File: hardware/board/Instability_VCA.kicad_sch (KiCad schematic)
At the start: 30 parts

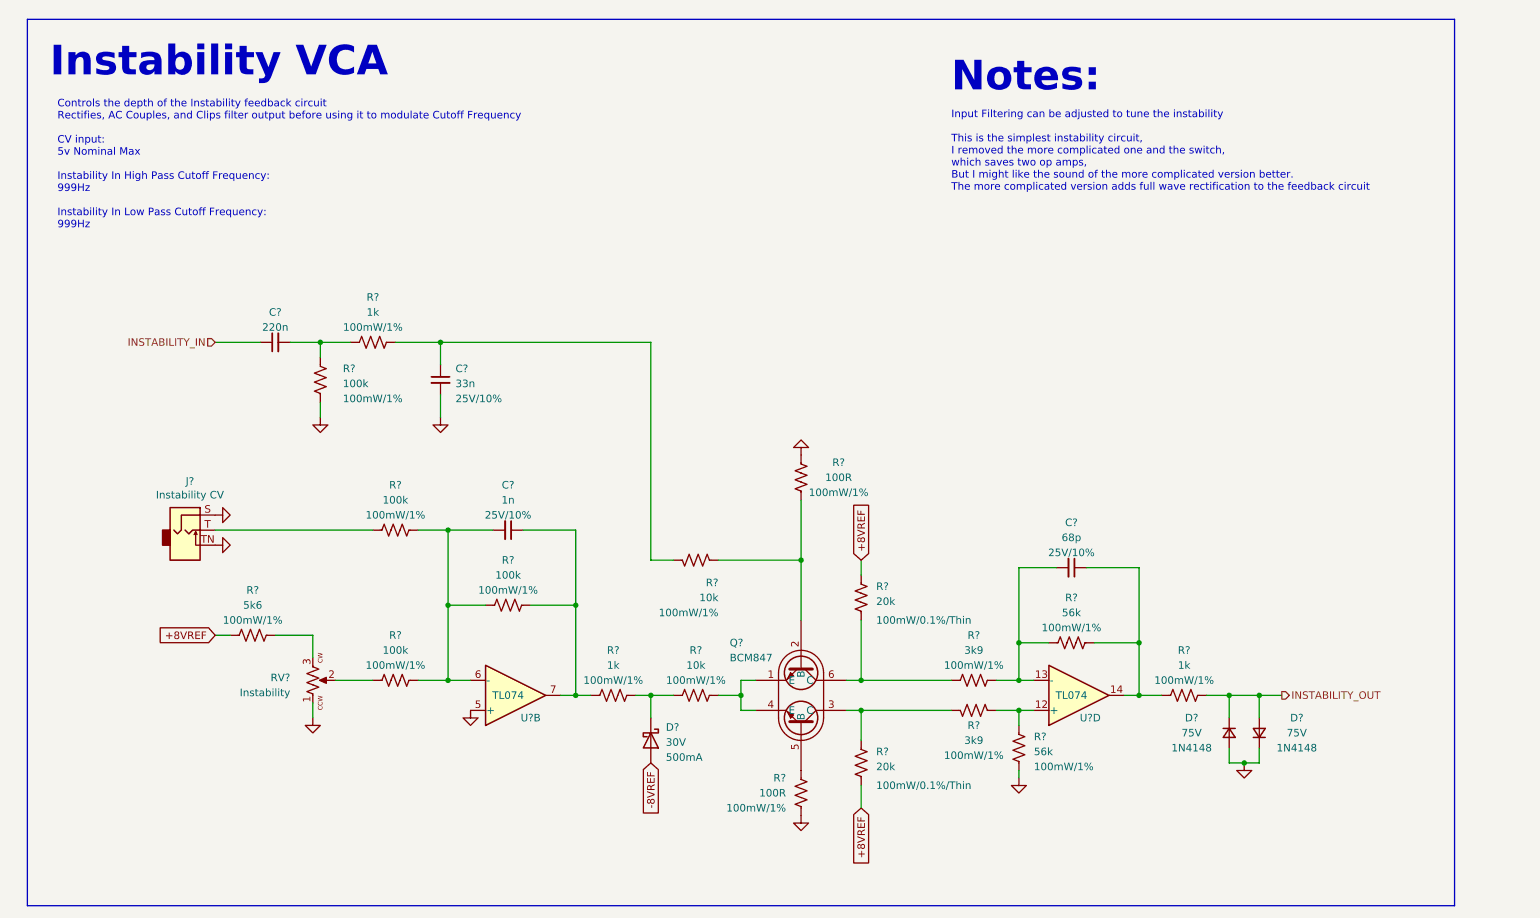
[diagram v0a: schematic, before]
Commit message: Schematic getting closer to being finished
Schematic should be close to being ready to assign MPNs.
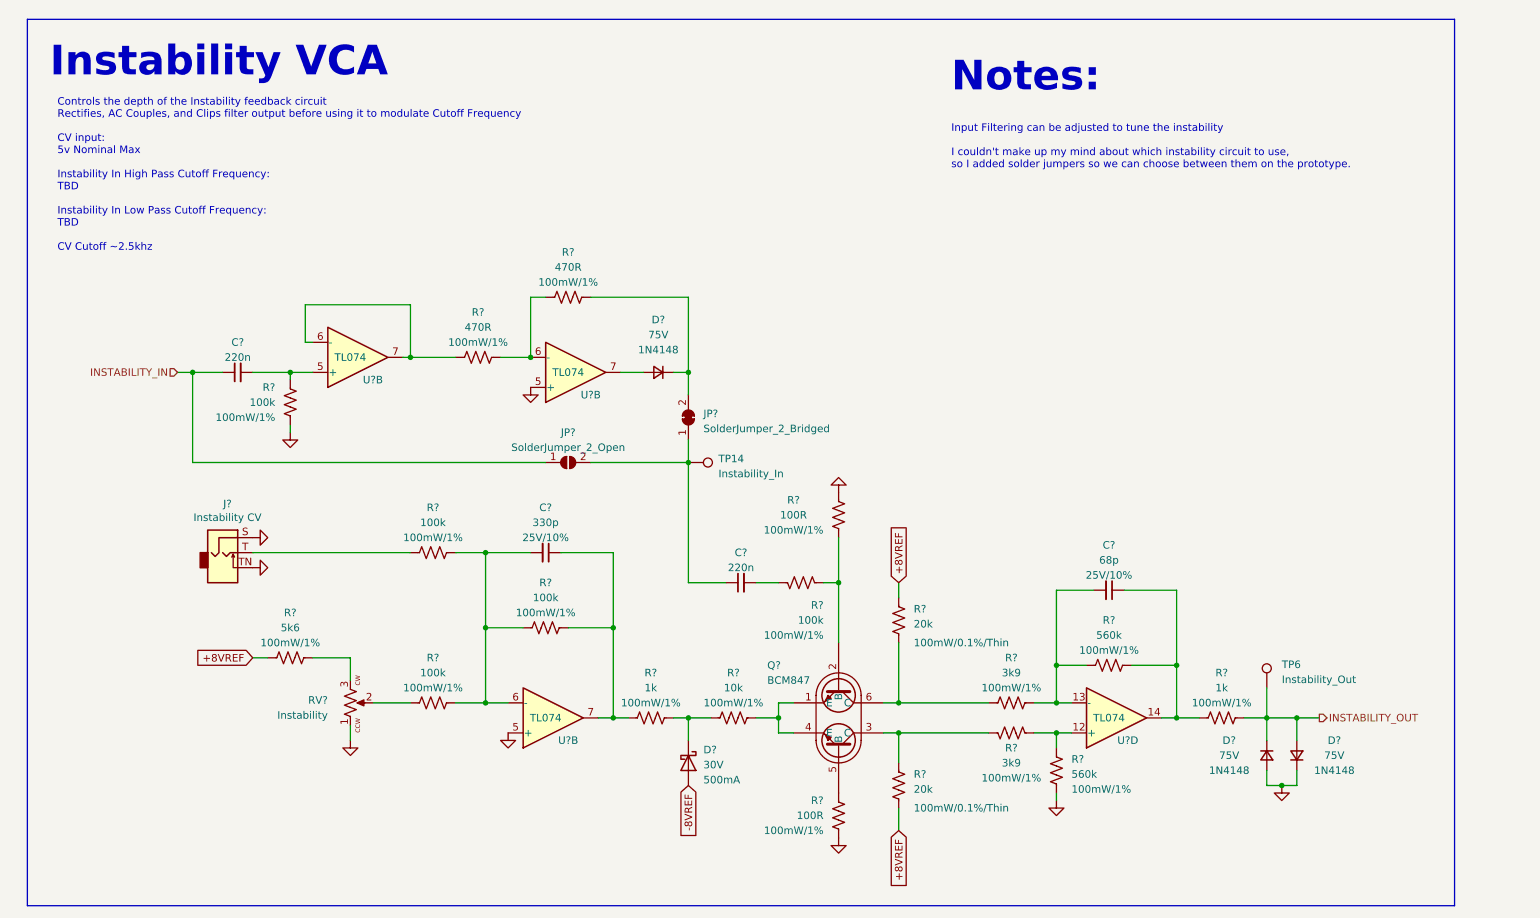
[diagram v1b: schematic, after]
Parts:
- removed C?: 33n, winterbloom:C_0603_HandSolder, symbol Device:C_Small
- removed R?: 100k, winterbloom:R_0603_HandSolder, symbol Device:R_US
- removed R?: 1k, winterbloom:R_0603_HandSolder, symbol Device:R_US
- added C?: 220n, winterbloom:C_0603_HandSolder, symbol Device:C_Small
- added D?: 75V, Diode_SMD:D_SOD-123, symbol Device:D_Small
- added JP?: SolderJumper_2_Bridged, symbol Jumper:SolderJumper_2_Bridged
- added JP?: SolderJumper_2_Open, symbol Jumper:SolderJumper_2_Open
- added R? (x2): 470R, winterbloom:R_0603_HandSolder, symbol Device:R_US
- added R?: 100k, winterbloom:R_0603_HandSolder, symbol Device:R_US
- added TP14: Instability_In, symbol Connector:TestPoint
- added TP6: Instability_Out, symbol Connector:TestPoint
- added U? (x2): TL074, Package_SO:TSSOP-14_4.4x5mm_P0.65mm, symbol winterbloom:TL074
- C?: value 1n -> 330p
- R? (x2): value 56k -> 560k
- R?: value 10k -> 100k
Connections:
- net GND: now also R?.1, U?.5 (+)
- net INSTABILITY_IN: now also C?.1, JP?.1 (A); no longer C?.1
- net INSTABILITY_OUT: now also TP6.1
- net at C?.2: now also R?.1
- new net: R?.1, R?.2, U?.6 (-)
- new net: D?.2 (A), U?.7
- new net: C?.1, JP?.1 (A), JP?.2 (B), TP14.1
- new net: D?.1 (K), JP?.2 (B), R?.1
- new net: C?.2, R?.2, U?.5 (+)
- new net: R?.2, U?.6 (-), U?.7
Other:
- note added: "Controls the depth of the Instability feedback circuit Rectifies, AC Couples, and Clips filter output before using it to modulate Cutoff Frequency CV input: 5v Nominal Max Instability In High Pass Cutoff Frequency: TBD Instability In Low Pass Cutoff Frequency: TBD CV Cutoff ~2.5khz"
- note added: "Input Filtering can be adjusted to tune the instability I couldn't make up my mind about which instability circuit to use, so I added solder jumpers so we can choose between them on the prototype."
- note removed: "Controls the depth of the Instability feedback circuit Rectifies, AC Couples, and Clips filter output before using it to modulate Cutoff Frequency CV input: 5v Nominal Max Instability In High Pass Cutoff Frequency: 999Hz Instability In Low Pass Cutoff Frequency: 999Hz"
- note removed: "Input Filtering can be adjusted to tune the instability This is the simplest instability circuit, I removed the more complicated one and the switch, which saves two op amps, But I might like the sound of the more complicated version better. The more complicated version adds full wave rectification to the feedback circuit"
- moved on the sheet: C?, D?, J?, Q?, R?, RV?, U?B, U?D

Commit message: BOM Consolidation
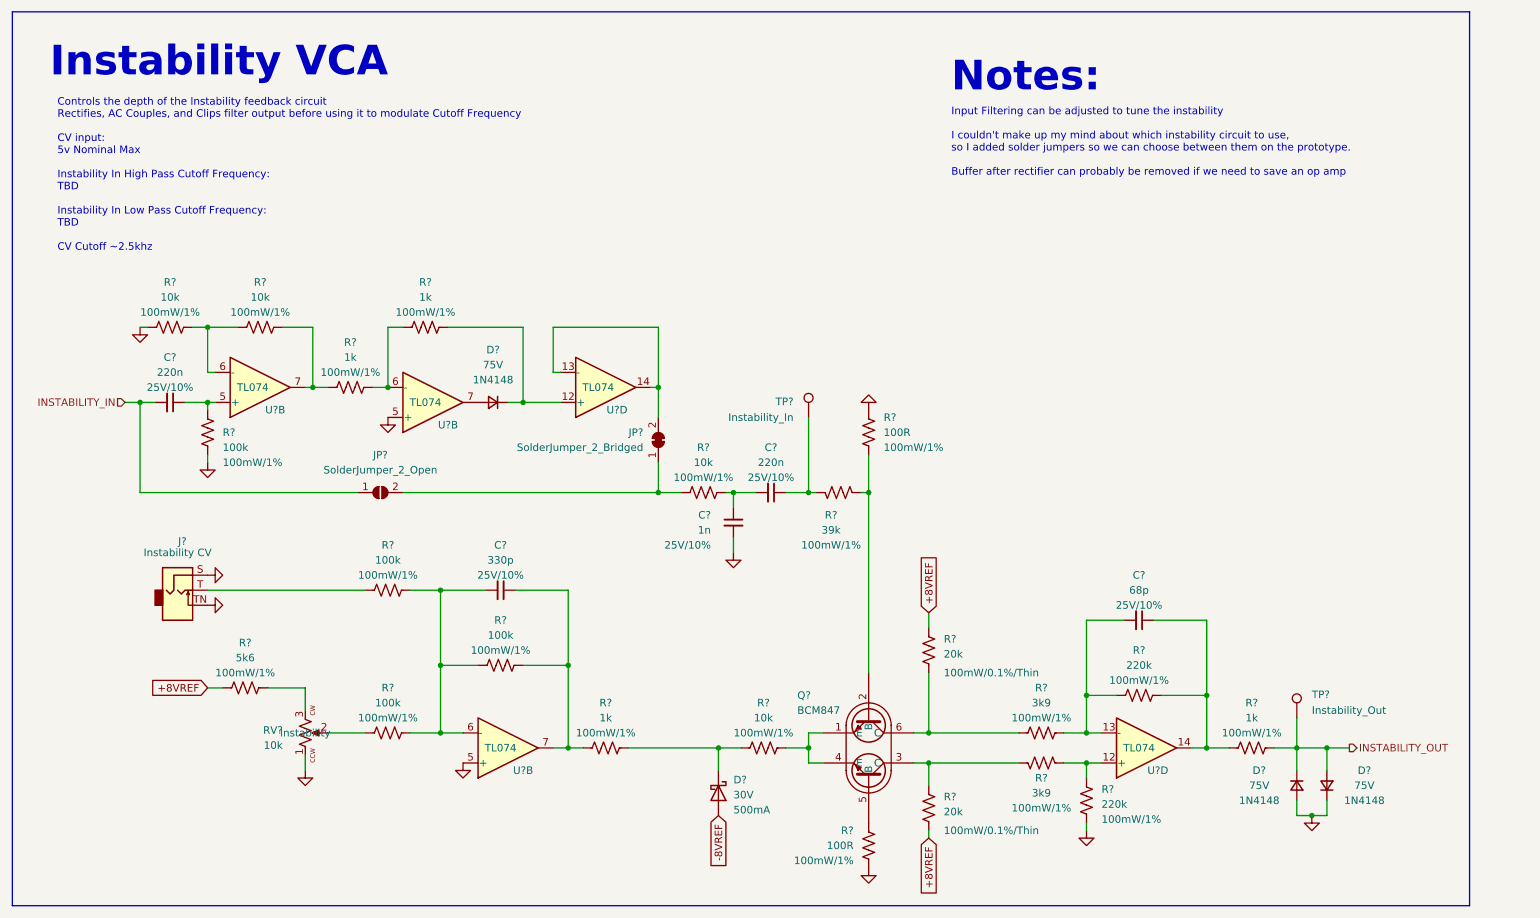
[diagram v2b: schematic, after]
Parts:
- removed C? (x2): 220n, winterbloom:C_0603_HandSolder, symbol Device:C_Small
- added C? (x2): 220n, winterbloom:C_0603_HandSolder, symbol Device:C_Small
- added C?: 1n, winterbloom:C_0603_HandSolder, symbol Device:C_Small
- added R? (x3): 10k, winterbloom:R_0603_HandSolder, symbol Device:R_US
- added U?: TL074, Package_SO:TSSOP-14_4.4x5mm_P0.65mm, symbol winterbloom:TL074
- J?: value Instability CV -> ~; Name (none) -> Instability CV
- R? (x2): value 470R -> 1k
- R? (x2): value 560k -> 220k
- R?: value 100k -> 39k
- RV?: value Instability -> 10k; Name (none) -> Instability
- TP?: renamed from TP14; value Instability_In -> ~; Name (none) -> Instability_In
- TP?: renamed from TP6; value Instability_Out -> ~; Name (none) -> Instability_Out
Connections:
- net GND: now also C?.2, R?.2
- net INSTABILITY_IN: now also C?.2
- net at JP?.1 (A), JP?.2 (B): now also R?.2; no longer TP?.1
- net at R?.1: now also TP?.1, C?.1
- net at D?.1 (K), R?.1: now also U?.12 (+); no longer JP?.2 (B)
- net at R?.2, U?.5 (+): now also C?.1
- net at R?.2, U?.7: now also R?.1; no longer U?.6 (-)
- new net: R?.1, R?.2, U?.6 (-)
- new net: C?.1, C?.2, R?.1
- new net: JP?.2 (B), U?.13 (-), U?.14
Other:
- note added: "Input Filtering can be adjusted to tune the instability I couldn't make up my mind about which instability circuit to use, so I added solder jumpers so we can choose between them on the prototype. Buffer after rectifier can probably be removed if we need to save an op amp"
- note removed: "Input Filtering can be adjusted to tune the instability I couldn't make up my mind about which instability circuit to use, so I added solder jumpers so we can choose between them on the prototype."
- moved on the sheet: C?, D?, J?, JP?, Q?, R?, RV?, TP?, U?B, U?D

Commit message: Updates for LED Drivers
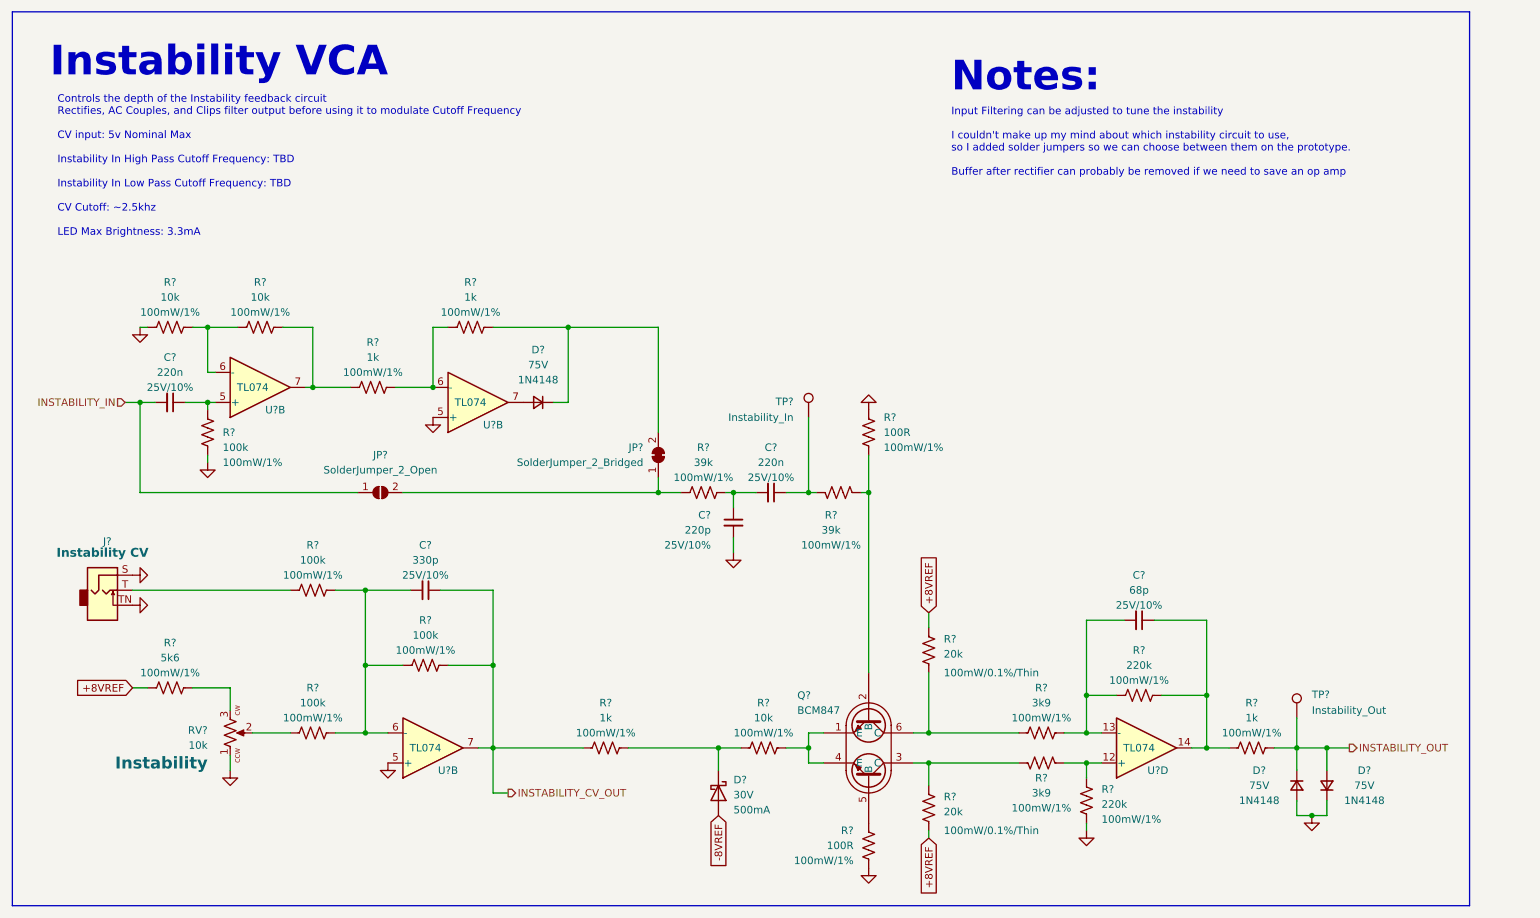
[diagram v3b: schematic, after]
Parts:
- removed U?: TL074, Package_SO:TSSOP-14_4.4x5mm_P0.65mm, symbol winterbloom:TL074
- C?: value 1n -> 220p
- R?: value 10k -> 39k
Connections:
- net INSTABILITY_CV_OUT: now reaches C?.1, R?.1, R?.2, U?.7
- net at JP?.2 (B): now also D?.1 (K), R?.1
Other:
- note added: "Controls the depth of the Instability feedback circuit Rectifies, AC Couples, and Clips filter output before using it to modulate Cutoff Frequency CV input: 5v Nominal Max Instability In High Pass Cutoff Frequency: TBD Instability In Low Pass Cutoff Frequency: TBD CV Cutoff: ~2.5khz LED Max Brightness: 3.3mA"
- note removed: "Controls the depth of the Instability feedback circuit Rectifies, AC Couples, and Clips filter output before using it to modulate Cutoff Frequency CV input: 5v Nominal Max Instability In High Pass Cutoff Frequency: TBD Instability In Low Pass Cutoff Frequency: TBD CV Cutoff ~2.5khz"
- moved on the sheet: C?, D?, J?, JP?, R?, RV?, U?B

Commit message: hardware: update schematic with footprints and preliminary MPNs
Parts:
- C? (x5): Notes 0603, 25V+, 10% -> (none); smd kit 1 -> (none)
- D? (x3): value 75V -> BAS315; footprint Diode_SMD:D_SOD-123 -> winterbloom:D_SOD-323; LCSC C81598 -> (none); MPN 1N4148W -> BAS316,115; Manufacturer ST(Semtech) -> (none); Notes (none) -> Clipping diode; Rating 1N4148 -> 1Vf @ 100mA
- D?: value 30V -> BAS315; footprint winterbloom:D_SOD-123+SOD-123F -> winterbloom:D_SOD-323; MPN (none) -> BAS316,115; Notes Any PMEGxxxxEGW part, 500mA If -> Clipping diode; Rating 500mA -> 1Vf @ 100mA; mpn PMEG2005EGWX -> (none); smd kit 1 -> (none)
- J?: mpn WQP-WQP518MA -> (none)
- JP701: renamed from JP?; footprint (none) -> Jumper:SolderJumper-2_P1.3mm_Open_RoundedPad1.0x1.5mm
- JP702: renamed from JP?; footprint (none) -> Jumper:SolderJumper-2_P1.3mm_Bridged_RoundedPad1.0x1.5mm
- Q?: LCSC C396099 -> (none); LCSC Extended YES -> (none); Manufacturer Nexperia -> (none)
- R? (x20): smd kit 1 -> (none)
- R? (x2): Rating 100mW/1% -> 100mW/1%/Thin; smd kit 1 -> (none)
- TP701, TP702: renamed from TP?; footprint (none) -> TestPoint:TestPoint_Pad_D1.5mm
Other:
- title: Diode Ladder Filter -> Neptune

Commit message: Very first component layout.
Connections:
- net GND: now also U?.5 (+); no longer U?.5 (+)
- net INSTABILITY_CV_OUT: now also U?.7; no longer U?.7
- net at C?.1, R?.2: now also U?.12 (+); no longer U?.5 (+)
- net at R?.1, R?.2: now also U?.6 (-); no longer U?.6 (-)
- net at U?.7: now also C?.1, R?.1, R?.2; no longer D?.2 (A)
- net at C?.2, R?.1, R?.1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: now also U?.6 (-); no longer U?.6 (-)
- net at R?.1, R?.2: now also U?.13 (-); no longer U?.6 (-)
- net at C?.2, R?.1, R?.2: now also U?.6 (-); no longer U?.13 (-)
- net at R?.1, R?.1: now also U?.5 (+); no longer U?.12 (+)
- net at R?.1, R?.2: now also U?.14; no longer U?.7
- new net: D?.2 (A), U?.7
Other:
- moved on the sheet: D?, U?B, U?D
